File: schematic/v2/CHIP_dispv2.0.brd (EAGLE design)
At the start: 40.9 x 49.8 mm, 38 parts, among them J1 2X20-CHIPB, J3 S2B-PH-SM4-TB, Q1 NPN-DTC114YUA, Q2 PNP-DTA114YUA, U1 LMR62421, U3 DS2431P, X1 FH12-40S-0.5SH

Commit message: added solder marks
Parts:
- moved U1 10.9 mm to (28.9, 26.6)
- moved C15 10.9 mm to (22.4, 38.4)
- moved C2 10.9 mm to (32.0, 33.7)
- moved C9 10.9 mm to (7.54, 43.0)
- moved L- 10.9 mm to (23.1, 48.0)
- moved Q1 10.9 mm to (32.4, 9.56)
- moved R+ 10.9 mm to (26.9, 43.4)
- moved R- 10.9 mm to (24.1, 43.4)
- moved R2 10.9 mm to (28.8, 23.1)
- moved R3 10.9 mm to (33.3, 23.1)
- moved R4 10.9 mm to (32.0, 39.1)
- moved SDIO 10.9 mm to (14.2, 41.7)
- moved C1 10.9 mm to (28.8, 20.8)
- moved C14 10.9 mm to (27.9, 39.1)
- moved C3 10.9 mm to (29.2, 16.3)
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
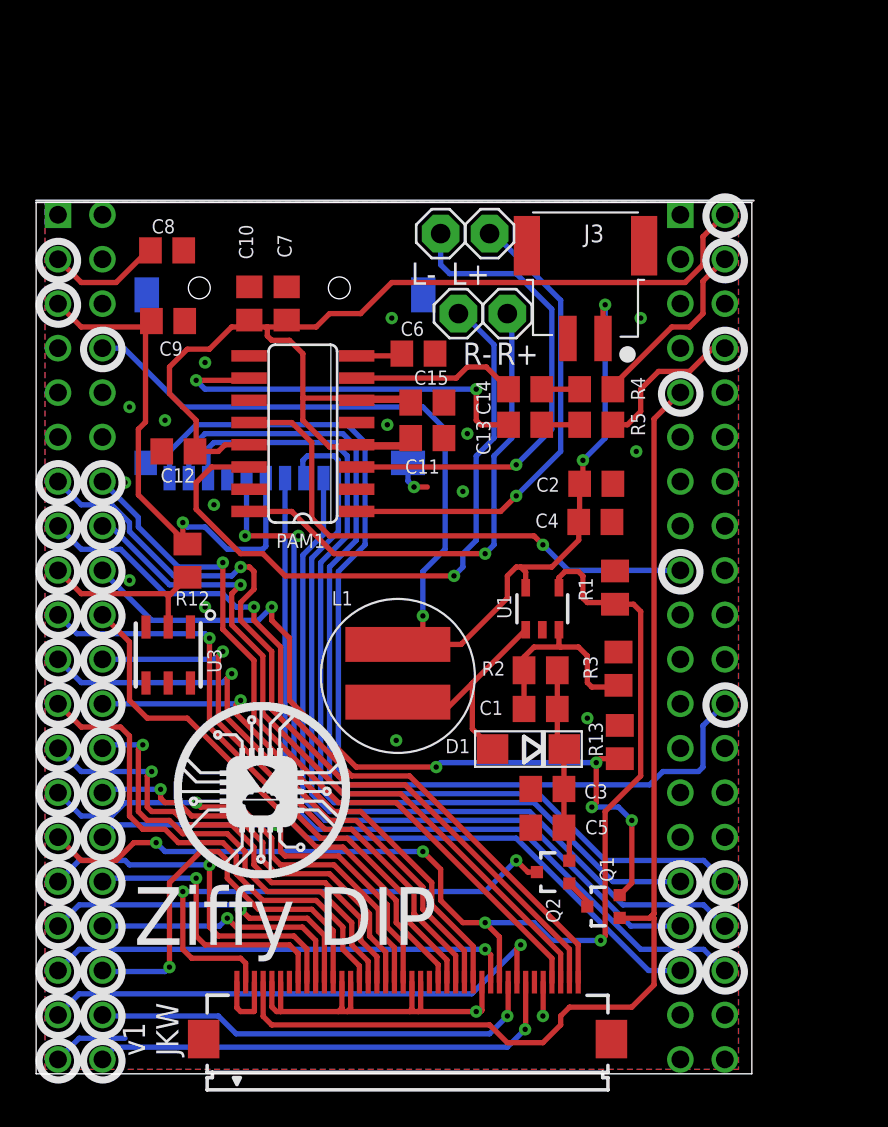
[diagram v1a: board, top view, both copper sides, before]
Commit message: moved sd to right
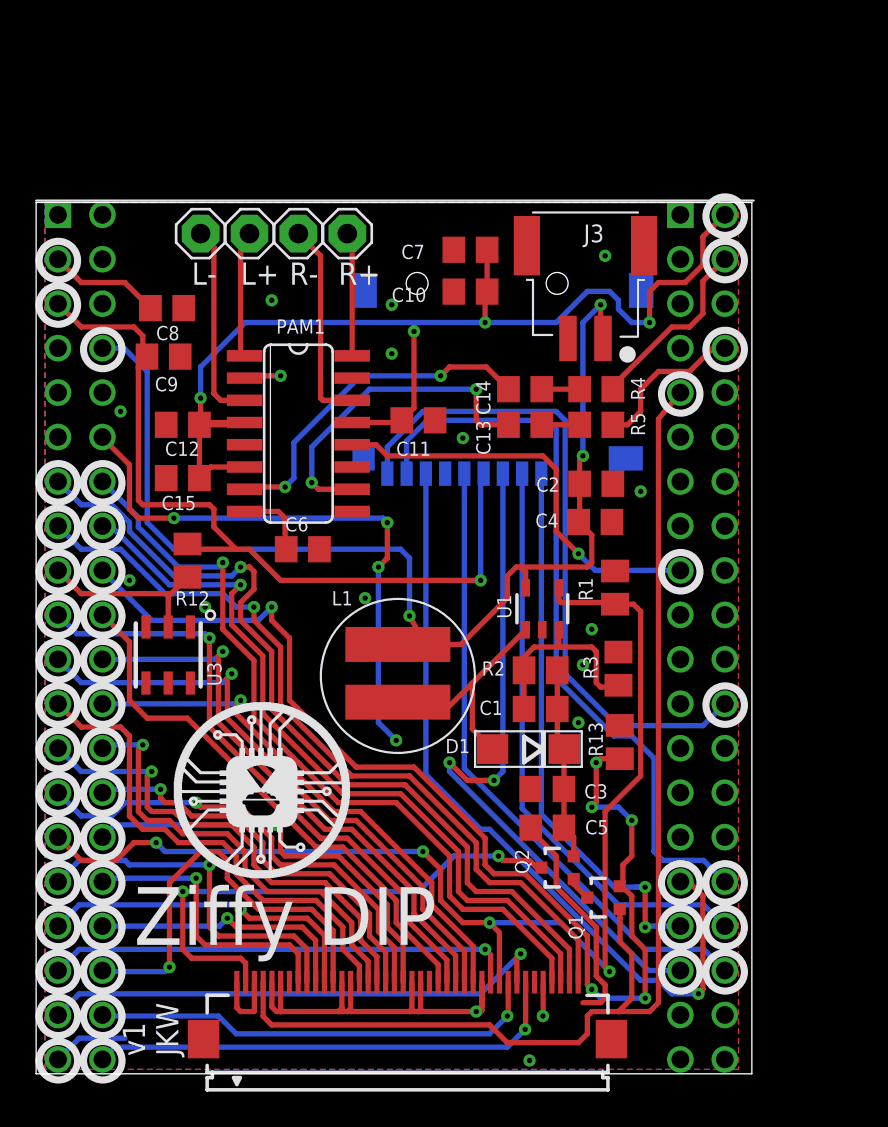
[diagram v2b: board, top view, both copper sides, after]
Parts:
- moved C15 14.6 mm to (8.38, 34.0), turned to 180 degrees
- moved L+ 13.7 mm to (12.2, 48.0)
- moved L- 13.7 mm to (9.40, 48.0)
- moved C6 13.0 mm to (15.2, 30.0)
- moved C10 12.7 mm to (24.8, 44.7), turned to 180 degrees
- moved SDIO 12.4 mm to (26.7, 41.9)
- moved C7 10.9 mm to (24.8, 47.1), turned to 180 degrees
- moved R+ 10.2 mm to (17.8, 48.0)
- moved R- 10.2 mm to (15.0, 48.0)
- moved C8 3.30 mm to (7.48, 43.7)
- moved C9 2.05 mm to (7.29, 41.0)
- moved C12 1.55 mm to (8.38, 37.1)
- moved C11 1.14 mm to (21.8, 37.3)
- moved Q1 0.51 mm to (32.4, 10.1)
- moved Q2 0.36 mm to (29.8, 11.8)
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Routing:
- net GND: track 36.6 -> 83.9 mm, vias 18 -> 21
- net N$35: track 38.1 -> 11.8 mm, vias 1 -> 0
- net N$34: track 28.9 -> 7.10 mm, vias 1 -> 0
- net N$45: track 59.0 -> 38.1 mm
- net N$32: track 27.4 -> 7.29 mm, vias 1 -> 0
- net PWM: track 47.4 -> 64.7 mm, vias 5 -> 6
- net N$33: track 28.1 -> 11.4 mm, vias 1 -> 0
- net VCC3V3: track 30.4 -> 46.8 mm
- net N$28: track 49.7 -> 33.5 mm
- net N$44: track 50.8 -> 36.5 mm, vias 2 -> 0
- net N$27: track 56.5 -> 42.9 mm
- net N$31: track 43.4 -> 32.3 mm, vias 0 -> 2
- net N$36: track 9.47 -> 19.7 mm, vias 0 -> 2
- net VCC5V: track 72.5 -> 64.7 mm, vias 0 -> 4
- net N$1: track 52.5 -> 45.3 mm, vias 0 -> 1
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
